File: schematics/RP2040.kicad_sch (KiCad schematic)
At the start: 36 parts, among them J1 USB_C_Receptacle_USB2.0, J2 SWD, J3 Conn_01x11, J4 Conn_01x11, J5 Conn_01x11, SW1 SW_Push, U1 W25Q128JVS, U2 USBLC6-2SC6, U3 RP2040, U4 XC6206PxxxMR-Regulator_Linear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

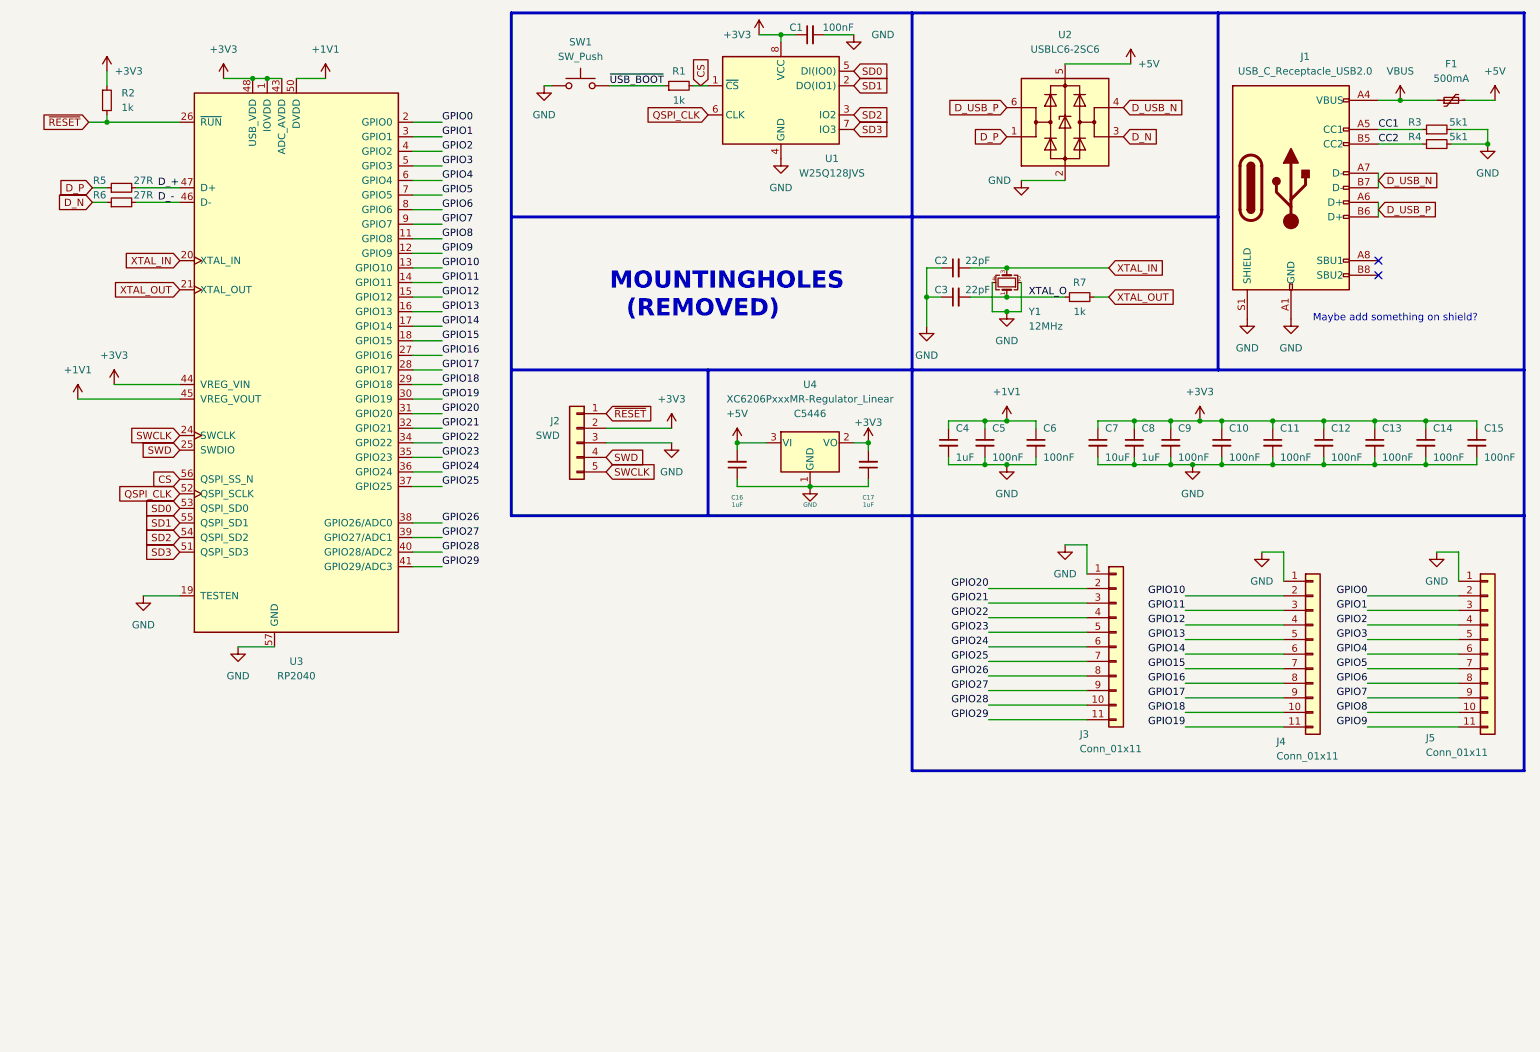
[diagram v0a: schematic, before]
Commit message: Change layout to better reflect what I like
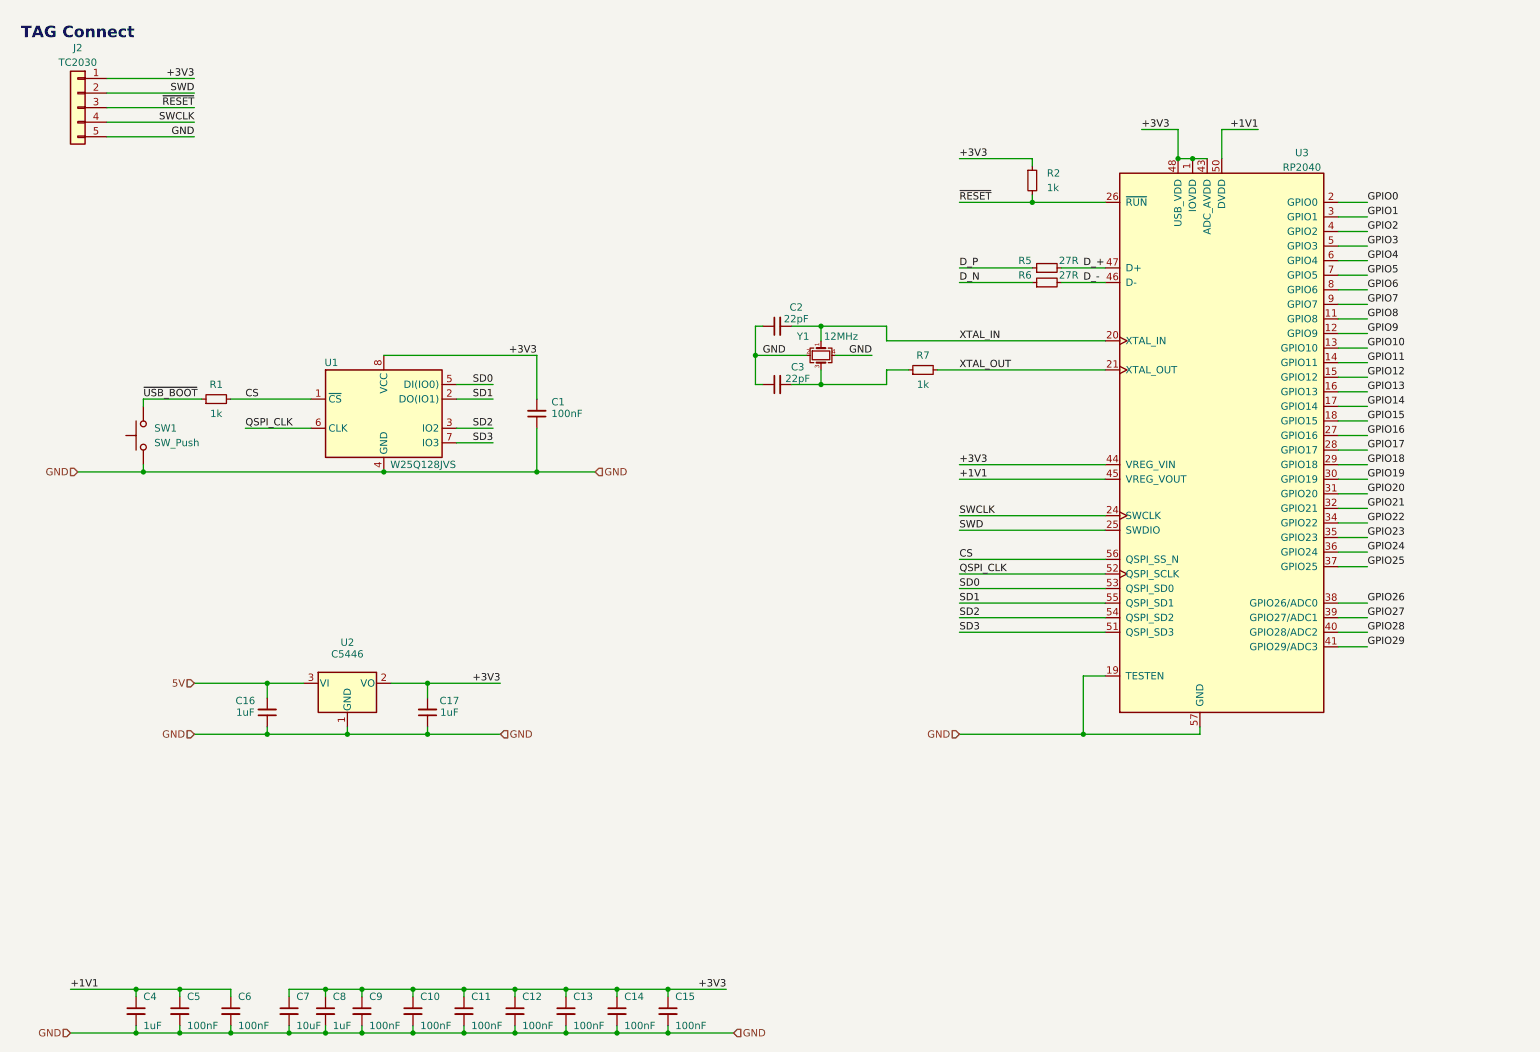
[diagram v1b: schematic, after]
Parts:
- removed F1: 500mA, Fuse:Fuse_1206_3216Metric, symbol Device:Polyfuse_Small
- removed J1: USB_C_Receptacle_USB2.0, Connector_USB:USB_C_Receptacle_HRO_TYPE-C-31-M-12, symbol Connector:USB_C_Receptacle_USB2.0
- removed J3, J4, J5: Conn_01x11, Connector_PinSocket_2.54mm:PinSocket_1x11_P2.54mm_Vertical, symbol Connector_Generic:Conn_01x11
- removed R3, R4: 5k1, Resistor_SMD:R_0402_1005Metric, symbol Device:R_Small
- removed U2: USBLC6-2SC6, Package_TO_SOT_SMD:SOT-23-6, symbol Power_Protection:USBLC6-2SC6
- removed U4: XC6206PxxxMR-Regulator_Linear, Package_TO_SOT_SMD:SOT-23, symbol kicad-keyboard-parts:XC6206PxxxMR-Regulator_Linear
- added U2: XC6206PxxxMR-Regulator_Linear, Package_TO_SOT_SMD:SOT-23, symbol kicad-keyboard-parts:XC6206PxxxMR-Regulator_Linear
- J2: value SWD -> TC2030; footprint Connector_PinSocket_2.54mm:PinSocket_1x05_P2.54mm_Vertical -> Connector:Tag-Connect_TC2030-IDC-NL_2x03_P1.27mm_Vertical
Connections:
- net GND: now also C1.1, J2.5 (Pin_5), U2.1 (GND); no longer C1.2, J2.3 (Pin_3)
- net SWCLK: now also J2.4 (Pin_4); no longer J2.5 (Pin_5)
- net SWD: now also J2.2 (Pin_2); no longer J2.4 (Pin_4)
- net XTAL_IN: now also Y1.1; no longer Y1.3
- net ~{RESET}: now also J2.3 (Pin_3); no longer J2.1 (Pin_1)
- net +1V1 renamed DVDD
- net +3V3 renamed IOVDD
- net IOVDD: now also C1.2, J2.1 (Pin_1), U2.2 (VO); no longer C1.1, J2.2 (Pin_2)
- net +5V renamed 5V
- net 5V: now also U2.3 (VI)
- net XTAL_O: no longer names the net of C3.2, R7.1
- net XTAL_O: now also Y1.3; no longer Y1.1
- no-connect marks 2 -> 0
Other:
- note added: "TAG Connect"
- note removed: "MOUNTINGHOLES (REMOVED)"
- note removed: "Maybe add something on shield?"
- moved on the sheet: C1, C10, C11, C12, C13, C14, C15, C4, C5, C6, C7, C8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
